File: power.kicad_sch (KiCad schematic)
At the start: 33 parts, among them U2 LMR51635XDDCR, U3 AMS1117

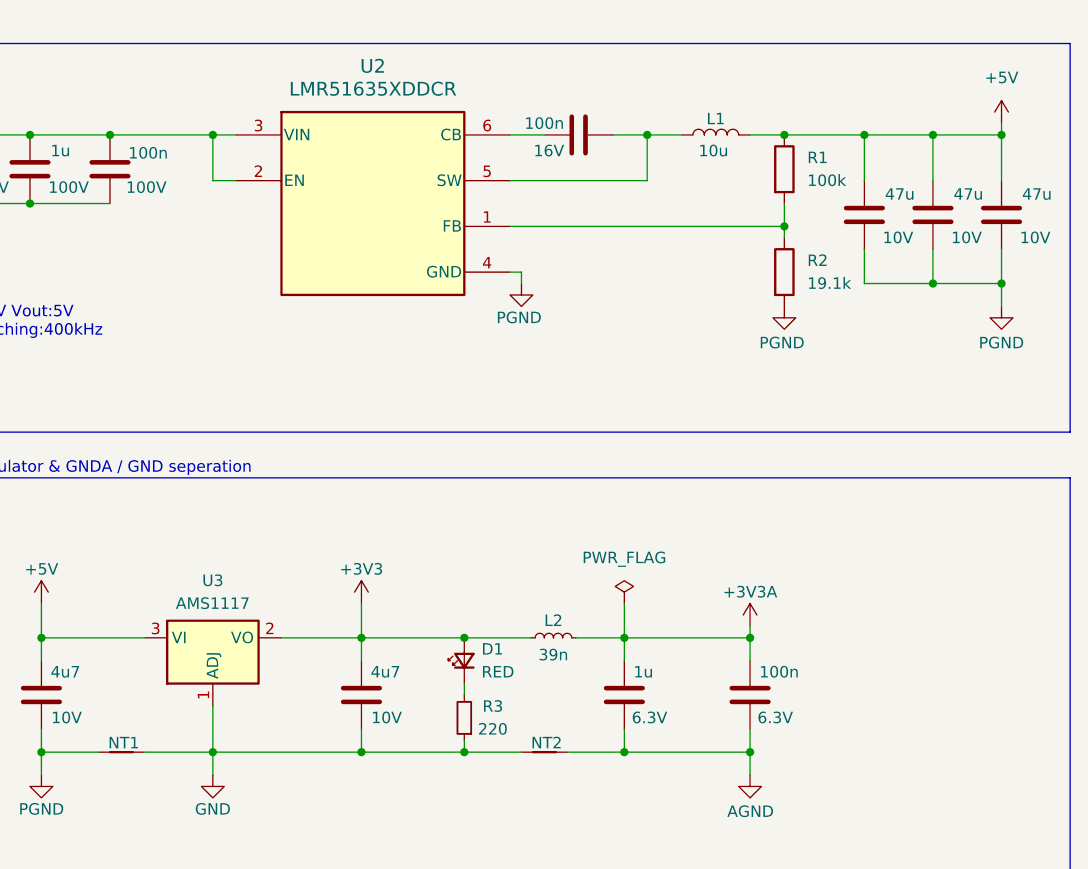
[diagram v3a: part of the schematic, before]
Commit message: added Net Classes  added +5V supply selection header
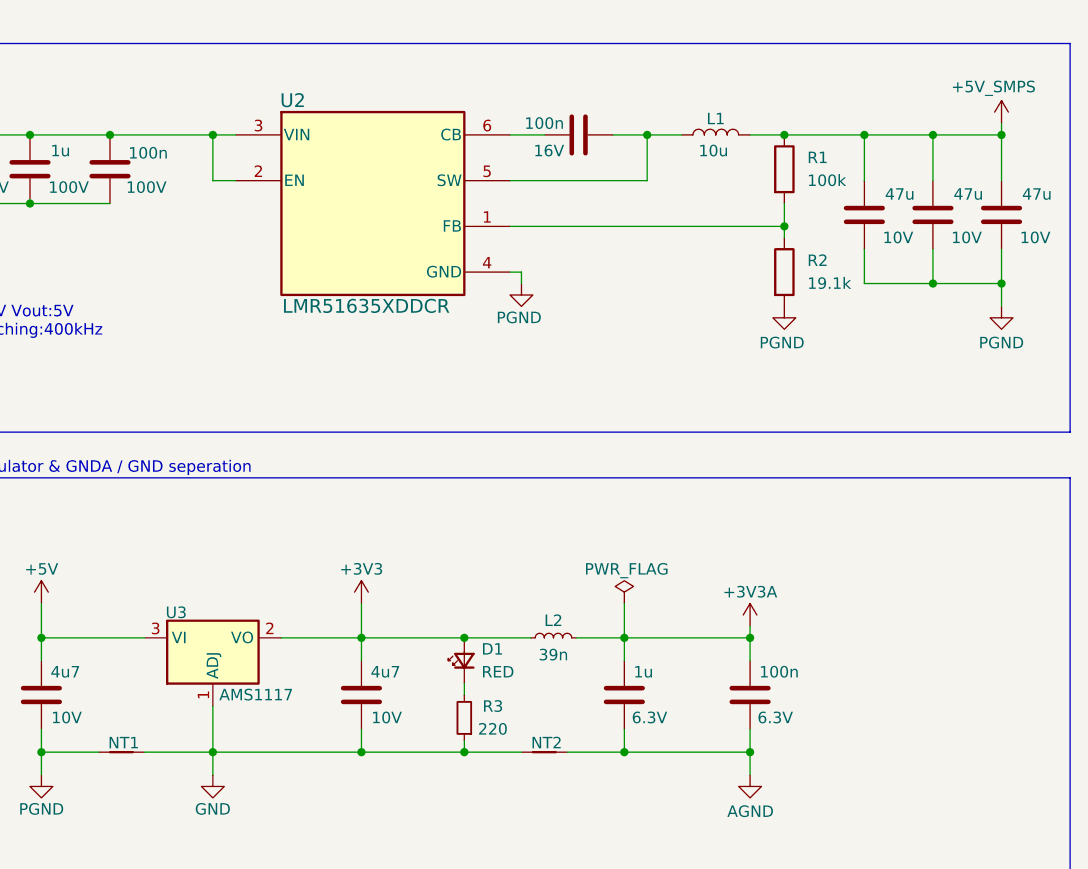
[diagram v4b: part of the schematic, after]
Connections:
- net +5V: no longer C6.1, C82.1, C86.1, L1.2, R1.1
- new net +5V_SMPS: C6.1, C82.1, C86.1, L1.2, R1.1
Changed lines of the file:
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@@
 		(on_board yes)
 		(dnp no)
-		(fields_autoplaced yes)
 		(property "Reference" "#PWR05"
 			(at 144.78 27.94 0)
@@
 			)
 		)
-		(property "Value" "+5V"
-			(at 144.78 19.05 0)
+		(property "Value" "+5V_SMPS"
+			(at 139.192 20.066 0)
 			(effects
 				(font
 					(size 1.27 1.27)
 				)
+				(justify left)
 			)
 		)
@@
 		(on_board yes)
 		(dnp no)
-		(fields_autoplaced yes)
 		(property "Reference" "#FLG02"
 			(at 102.87 75.565 0)
@@
 		)
 		(property "Value" "PWR_FLAG"
-			(at 102.87 72.39 0)
+			(at 103.124 73.66 0)
 			(effects
 				(font
@@
 		(on_board yes)
 		(dnp no)
-		(fields_autoplaced yes)
 		(property "Reference" "U2"
-			(at 74.93 17.78 0)
+			(at 66.04 21.59 0)
 			(effects
 				(font
@@
 		)
 		(property "Value" "LMR51635XDDCR"
-			(at 74.93 20.32 0)
+			(at 74.168 44.45 0)
 			(effects
 				(font
@@
 		(on_board yes)
 		(dnp no)
-		(fields_autoplaced yes)
 		(property "Reference" "U3"
-			(at 57.15 74.93 0)
+			(at 53.086 78.486 0)
 			(effects
 				(font
@@
 		)
 		(property "Value" "AMS1117"
-			(at 57.15 77.47 0)
+			(at 61.976 87.63 0)
 			(effects
 				(font

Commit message: WiP layout
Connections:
- net SW_FB: now reaches R1.2, R2.1, U2.1 (FB)
- net SW_SMPS: now reaches C5.2, L1.1, U2.5 (SW)
- net SW_CB: now reaches C5.1, U2.6 (CB)
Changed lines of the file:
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@@
+		)
+	)
+	(label "SW_FB"
+		(at 101.6 35.56 0)
+		(effects
+			(font
+				(size 1.27 1.27)
+			)
+			(justify left bottom)
+		)
+	)
+	(label "SW_CB"
+		(at 91.44 25.4 90)
+		(effects
+			(font
+				(size 1.27 1.27)
+			)
+			(justify left bottom)
+		)
+	)
+	(label "SW_SMPS"
+		(at 101.6 25.4 0)
+		(effects
+			(font
+				(size 1.27 1.27)
+			)
+			(justify left bottom)
 		)
 	)

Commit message: WiP layout
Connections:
- net +5V_SMPS is gone; now on net +5V: C6.1, C82.1, C86.1, L1.2, R1.1
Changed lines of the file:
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@@
 			)
 		)
-		(property "Value" "+5V_SMPS"
-			(at 139.192 20.066 0)
+		(property "Value" "+5V"
+			(at 142.748 20.574 0)
 			(effects
 				(font

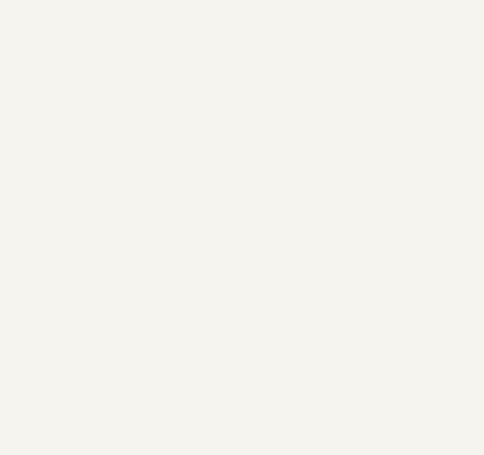
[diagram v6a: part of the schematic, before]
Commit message: added cooling channel symbol, footprint and 3D model
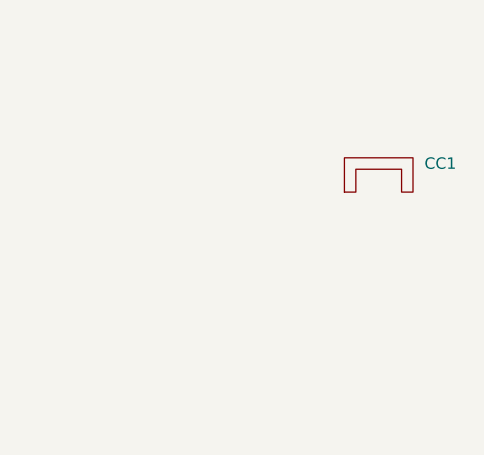
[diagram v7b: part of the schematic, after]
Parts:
- added CC1: ~, NanoGaN:CoolingChannel, symbol NanoGaN:CoolingChannel
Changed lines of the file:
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@@
+	)
+	(symbol
+		(lib_id "NanoGaN:CoolingChannel")
+		(at 259.08 30.48 0)
+		(unit 1)
+		(exclude_from_sim no)
+		(in_bom yes)
+		(on_board yes)
+		(dnp no)
+		(fields_autoplaced yes)
+		(property "Reference" "CC1"
+			(at 264.16 28.5749 0)
+			(effects
+				(font
+					(size 1.27 1.27)
+				)
+				(justify left)
+			)
+		)
+		(property "Value" "~"
+			(at 264.16 31.1149 0)
+			(effects
+				(font
+					(size 1.27 1.27)
+				)
+				(justify left)
+			)
+		)
+		(property "Footprint" "NanoGaN:CoolingChannel"
+			(at 259.08 30.48 0)
+			(effects
+				(font
+					(size 1.27 1.27)
+				)
+				(hide yes)
+			)
+		)
+		(property "Datasheet" ""
+			(at 259.08 30.48 0)
+			(effects
+				(font
+					(size 1.27 1.27)
+				)
+				(hide yes)
+			)
+		)
+		(property "Description" ""
+			(at 259.08 30.48 0)
+			(effects
+				(font
+					(size 1.27 1.27)
+				)
+				(hide yes)
+			)
+		)
+		(instances
+			(project ""
+				(path "/aa8a494f-605e-4a00-9d3c-daec94709fcb/2aff88eb-0d92-4253-8876-ba05112be4d6"
+					(reference "CC1")
+					(unit 1)
+				)
+			)
+		)
 	)
 	(symbol

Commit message: added the first draft of the layout
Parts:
- removed C44, C81: 150u, Capacitor_SMD:CP_Elec_10x10.5, symbol NanoGaN:C_Polarized_FZ1J221M1313
- removed CC1: ~, NanoGaN:CoolingChannel, symbol NanoGaN:CoolingChannel
- added C37, C40: 4u7, Capacitor_SMD:C_0402_1005Metric, symbol Device:C
- added C68: 1u, Capacitor_SMD:C_1206_3216Metric, symbol Device:C
- added C81, C88, C90: 100n, Capacitor_SMD:C_0805_2012Metric, symbol Device:C
- C11, C12, C13, C14, C27, C35: value 150u -> 470u; footprint Capacitor_SMD:CP_Elec_10x10.5 -> Capacitor_THT:CP_Radial_D12.5mm_P5.00mm; LCSC C22383765 -> (none); Voltage Rating 63V -> 80V
- C18: footprint Capacitor_SMD:C_0201_0603Metric -> Capacitor_SMD:C_0402_1005Metric; LCSC C541214 -> (none); now not fitted; now left out of the parts list
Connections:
- net +3V3: now also C37.1, C40.1
- net GND: now also C37.2, C40.2
- net PGND: now also C68.2, C81.2, C88.2, C90.2
- net U_DC: now also C68.1, C81.1, C88.1, C90.1
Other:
- note added: "Extra capacitors for improving switching performance."
- moved on the sheet: D1, L2, NT2, R3
